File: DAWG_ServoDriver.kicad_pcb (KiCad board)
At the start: 2 copper layers, 70 x 84 mm, 155 parts, among them CN10 Conn_02x19_Odd_Even, CN7 Conn_02x19_Odd_Even, IC1 DRV8251ADDAR, IC2 DRV8251ADDAR, IC3 DRV8251ADDAR, IC4 DRV8251ADDAR, J1 Conn_01x05, J10 Screw_Terminal_01x02, J11 Conn_01x10, J12 Conn_01x08, J13 Conn_01x05, J14 Conn_01x06, J15 Conn_01x08, J16 Screw_Terminal_01x02, J17 Conn_01x03, J18 Conn_01x03, J19 Conn_01x03, J2 Screw_Terminal_01x02, J20 Conn_01x03, J21 Conn_01x03, J22 Conn_01x03, J23 Conn_01x03, J24 Conn_01x03, J25 Conn_01x03, J26 Conn_01x03, J27 Conn_01x03, J28 Conn_01x03, J29 Conn_01x03, J3 Conn_01x05, J30 Conn_01x03, J31 Conn_01x03, J32 Conn_01x03, J33 Conn_01x03, J34 Conn_01x03, J35 Conn_01x03, J36 Conn_01x03, J4 Conn_01x04_Pin, J5 Screw_Terminal_01x02, J6 Conn_01x03, J7 Screw_Terminal_01x02, J8 Screw_Terminal_01x02, J9 Conn_01x05, Q1 BSS138, Q10 BSS138, Q11 BSS138, Q12 BSS138, Q13 BSS138, Q14 BSS138, Q15 BSS138, Q16 BSS138, Q17 BSS138, Q18 BSS138, Q19 BSS138, Q2 BSS138, Q20 BSS138, Q3 BSS138, Q4 BSS138, Q5 BSS138, Q6 BSS138, Q7 BSS138, Q8 BSS138, Q9 BSS138, SW1 SW_Push, U1 TPS62177DQC, U2 STM32G431C8Tx, U3 LD1117S12TR_SOT223, U4 ICM-20602, U5 ICM-20602, Y1 Crystal_GND24

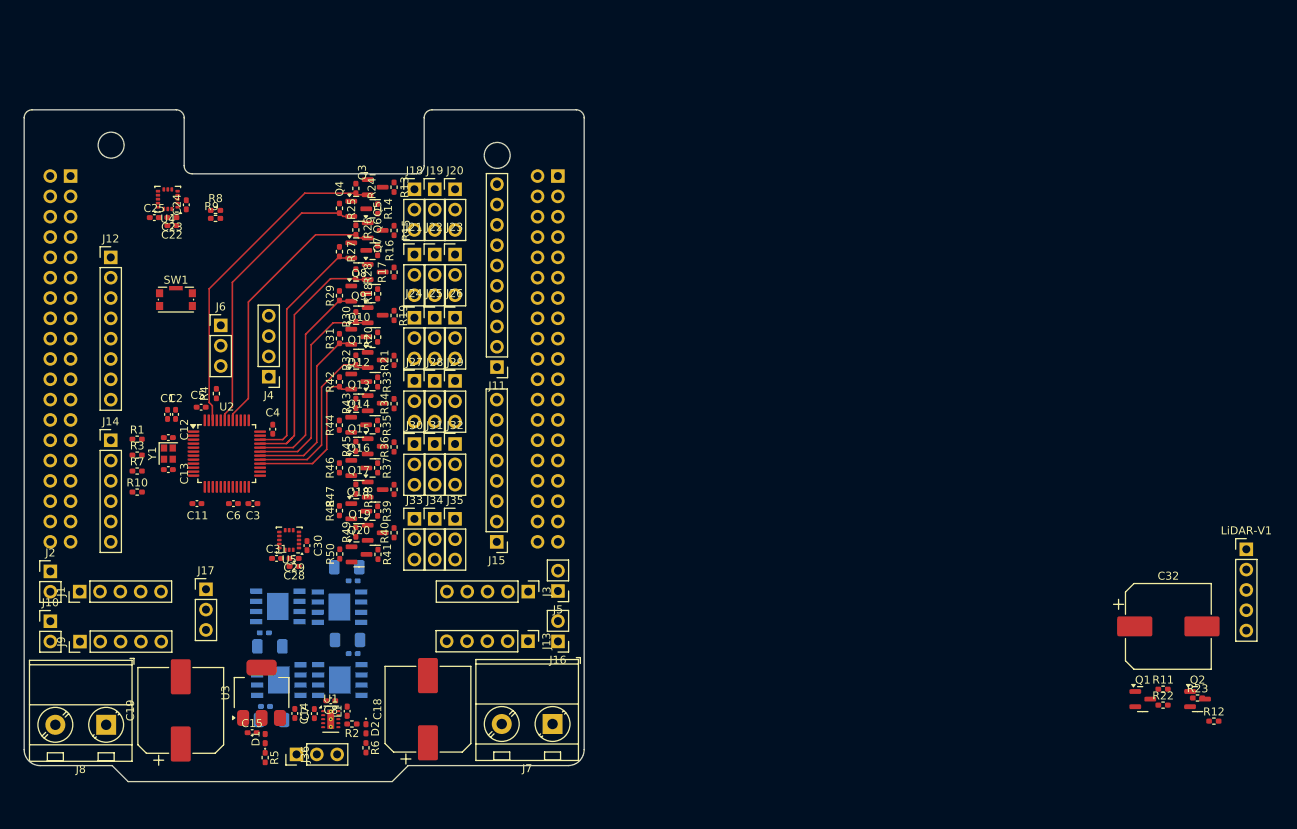
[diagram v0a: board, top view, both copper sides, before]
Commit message: Key components placed, Onion board begins.
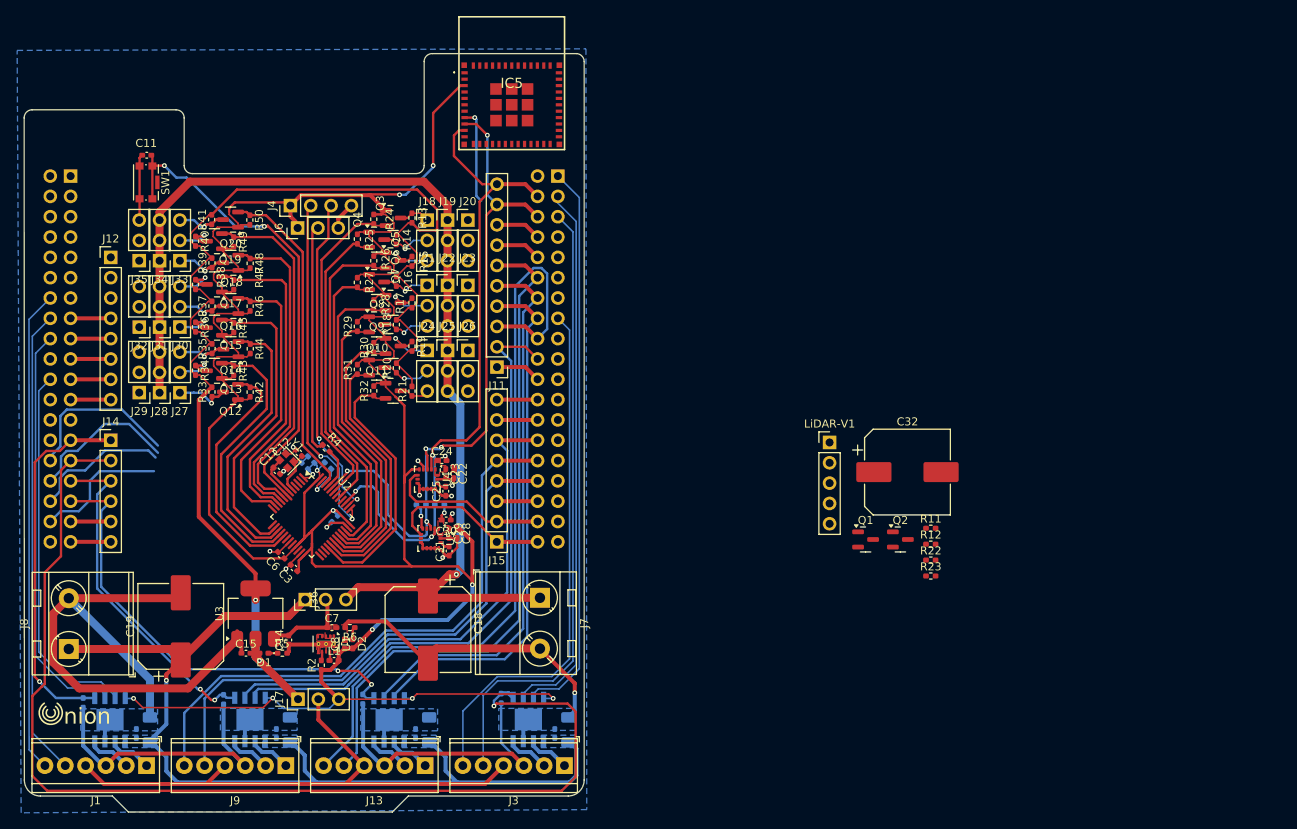
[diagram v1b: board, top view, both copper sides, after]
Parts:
- removed J10, J16, J2, J5: Screw_Terminal_01x02, Connector_PinHeader_2.54mm:PinHeader_1x02_P2.54mm_Vertical
- added IC5: ESP32-PICO-MINI-02-N8R2, Package_DFN_QFN:ESP32PICOMINI02N8R2, F.Cu at (84.0, 73.4)
- C1, C2, C4, C5, R1, R10, R3, R7, R8, R9: moved to B.Cu
- J1, J13, J3, J9: value Conn_01x05 -> Screw_Terminal_01x06; footprint Connector_PinHeader_2.54mm:PinHeader_1x05_P2.54mm_Vertical -> TerminalBlock_TE-Connectivity:TerminalBlock_TE_282834-6_1x06_P2.54mm_Horizontal
- moved R3 54.7 mm to (82.7, 147.6), turned to 90 degrees
- moved LiDAR-V1 53.8 mm to (123.8, 115.6)
- moved J35 51.0 mm to (37.5, 92.9), turned to 180 degrees
- moved C25 50.0 mm to (75.8, 121.7), turned to 90 degrees
- moved U4 47.7 mm to (73.5, 120.2), turned to -90 degrees
- moved J34 47.2 mm to (40.0, 92.9), turned to 180 degrees
- moved C22 46.9 mm to (76.8, 119.5), turned to -90 degrees
- moved C23 46.9 mm to (75.8, 119.5), turned to -90 degrees
- moved R41 46.7 mm to (46.5, 87.8), turned to 90 degrees
- moved R9 45.4 mm to (75.0, 123.4)
- moved C24 45.2 mm to (75.3, 117.9), turned to 0 degrees
- moved R8 44.9 mm to (72.7, 123.4), turned to 0 degrees
- moved Q20 44.8 mm to (48.9, 87.8), turned to 180 degrees
- moved R40 44.1 mm to (44.5, 90.5), turned to -90 degrees
- moved C11 44.0 mm to (38.4, 79.7), turned to 0 degrees
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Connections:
- net /I2C3_SCL renamed /I2C1_SCL_5V
- CN10 pad 1: unconnected-(CN10-Pin_1-Pad1) -> /PWM3/2_M2
- CN10 pad 10: unconnected-(CN10-Pin_10-Pad10) -> GND
- CN10 pad 11: /Mtr1_EncoderA -> unconnected-(CN10-Pin_11-Pad11)
- CN10 pad 12: unconnected-(CN10-Pin_12-Pad12) -> /Mtr4_EncoderA
- CN10 pad 13: /PWM2/1_M1 -> unconnected-(CN10-Pin_13-Pad13)
- CN10 pad 14: unconnected-(CN10-Pin_14-Pad14) -> /PWM2/3_M4
- CN10 pad 15: /PWM3/1_M1 -> /Mtr2_EncoderB
- CN10 pad 16: /Mtr1_EncoderZ -> /PWM3/2_M4
- CN10 pad 17: /Mtr1_EncoderB -> unconnected-(CN10-Pin_17-Pad17)
- CN10 pad 18: unconnected-(CN10-Pin_18-Pad18) -> /Mtr4_EncoderB
- CN10 pad 19: /PWM3/2_M2 -> unconnected-(CN10-Pin_19-Pad19)
- CN10 pad 20: unconnected-(CN10-Pin_20-Pad20) -> /PWM1/1_M3
- CN10 pad 21: Net-(CN10-Pin_21) -> unconnected-(CN10-Pin_21-Pad21)
- CN10 pad 22: unconnected-(CN10-Pin_22-Pad22) -> Net-(CN10-Pin_22)
- CN10 pad 23: Net-(CN10-Pin_23) -> unconnected-(CN10-Pin_23-Pad23)
- CN10 pad 24: unconnected-(CN10-Pin_24-Pad24) -> Net-(CN10-Pin_24)
- CN10 pad 25: Net-(CN10-Pin_25) -> unconnected-(CN10-Pin_25-Pad25)
- CN10 pad 26: unconnected-(CN10-Pin_26-Pad26) -> Net-(CN10-Pin_26)
- CN10 pad 27: /PWM4/1_M2 -> unconnected-(CN10-Pin_27-Pad27)
- CN10 pad 28: unconnected-(CN10-Pin_28-Pad28) -> /PWM1/2_M3
- CN10 pad 29: /Mtr2_EncoderA -> unconnected-(CN10-Pin_29-Pad29)
- CN10 pad 3: /I2C1_SCL -> /PWM4/1_M2
- CN10 pad 30: unconnected-(CN10-Pin_30-Pad30) -> /Mtr3_EncoderB
- CN10 pad 31: /Mtr2_EncoderB -> unconnected-(CN10-Pin_31-Pad31)
- CN10 pad 32: unconnected-(CN10-Pin_32-Pad32) -> /Mtr3_EncoderA
- CN10 pad 33: Net-(CN10-Pin_33) -> unconnected-(CN10-Pin_33-Pad33)
- CN10 pad 34: unconnected-(CN10-Pin_34-Pad34) -> Net-(CN10-Pin_34)
- CN10 pad 35: /IMU2_INT -> unconnected-(CN10-Pin_35-Pad35)
- CN10 pad 36: unconnected-(CN10-Pin_36-Pad36) -> /IMU1_INT
- CN10 pad 37: /IMU1_INT -> unconnected-(CN10-Pin_37-Pad37)
- CN10 pad 38: unconnected-(CN10-Pin_38-Pad38) -> /IMU2_INT
- CN10 pad 4: unconnected-(CN10-Pin_4-Pad4) -> /I2C1_SCL
- CN10 pad 5: /I2C1_SDA -> /Mtr2_EncoderA
- CN10 pad 6: unconnected-(CN10-Pin_6-Pad6) -> /I2C1_SDA
- CN10 pad 7: Net-(CN10-Pin_7) -> unconnected-(CN10-Pin_7-Pad7)
- CN10 pad 8: unconnected-(CN10-Pin_8-Pad8) -> Net-(CN10-Pin_8)
- CN10 pad 9: GND -> unconnected-(CN10-Pin_9-Pad9)
- CN7 pad 14: unconnected-(CN7-Pin_14-Pad14) -> /Mtr1_EncoderB
- CN7 pad 15: unconnected-(CN7-Pin_15-Pad15) -> +3.3V
- CN7 pad 16: +3.3V -> /Mtr1_EncoderA
- CN7 pad 17: /Mtr4_EncoderA -> +5V
- CN7 pad 18: +5V -> /PWM2/1_M1
- CN7 pad 19: unconnected-(CN7-Pin_19-Pad19) -> GND
- CN7 pad 20: GND -> unconnected-(CN7-Pin_20-Pad20)
- CN7 pad 21: /Mtr4_EncoderB -> GND
- CN7 pad 22: GND -> /PWM3/1_M1
- CN7 pad 23: /Mtr4_EncoderZ -> Net-(CN7-Pin_23)
- CN7 pad 24: Net-(CN7-Pin_24) -> unconnected-(CN7-Pin_24-Pad24)
- CN7 pad 27: unconnected-(CN7-Pin_27-Pad27) -> /IsenseM1
- CN7 pad 28: /IsenseM1 -> unconnected-(CN7-Pin_28-Pad28)
- CN7 pad 29: unconnected-(CN7-Pin_29-Pad29) -> /IsenseM2
- CN7 pad 30: /IsenseM2 -> unconnected-(CN7-Pin_30-Pad30)
- CN7 pad 31: unconnected-(CN7-Pin_31-Pad31) -> /IsenseM3
- CN7 pad 32: /IsenseM3 -> unconnected-(CN7-Pin_32-Pad32)
- CN7 pad 33: unconnected-(CN7-Pin_33-Pad33) -> /IsenseM4
- CN7 pad 34: /IsenseM4 -> unconnected-(CN7-Pin_34-Pad34)
- CN7 pad 35: unconnected-(CN7-Pin_35-Pad35) -> Net-(CN7-Pin_35)
- CN7 pad 36: Net-(CN7-Pin_36) -> unconnected-(CN7-Pin_36-Pad36)
- CN7 pad 37: unconnected-(CN7-Pin_37-Pad37) -> Net-(CN7-Pin_37)
- CN7 pad 38: Net-(CN7-Pin_38) -> unconnected-(CN7-Pin_38-Pad38)
- IC1 pad 6: /V_M1B -> /V_M1A
- IC1 pad 8: /V_M1A -> /V_M1B
- IC2 pad 6: /V_M2B -> /V_M2A
- IC2 pad 8: /V_M2A -> /V_M2B
- IC3 pad 6: /V_M3B -> /V_M3A
- IC3 pad 8: /V_M3A -> /V_M3B
- IC4 pad 6: /V_M4B -> /V_M4A
- IC4 pad 8: /V_M4A -> /V_M4B
- J1 pad 1: /V_encoder -> /V_M1A
- J1 pad 2: /Mtr1_EncoderA -> /V_M1B
- J1 pad 3: /Mtr1_EncoderB -> GND
- J1 pad 4: /Mtr1_EncoderZ -> /V_encoder
- J1 pad 5: GND -> /Mtr1_EncoderA
- J11 pad 1: Net-(CN10-Pin_21) -> Net-(CN10-Pin_22)
- J11 pad 2: /PWM3/2_M2 -> /PWM1/1_M3
- J11 pad 3: /Mtr1_EncoderB -> /Mtr4_EncoderB
- J11 pad 4: /PWM3/1_M1 -> /PWM3/2_M4
- J11 pad 5: /PWM2/1_M1 -> /PWM2/3_M4
- J11 pad 6: /Mtr1_EncoderA -> /Mtr4_EncoderA
- J11 pad 8: Net-(CN10-Pin_7) -> Net-(CN10-Pin_8)
- J12 pad 8: Net-(CN7-Pin_24) -> Net-(CN7-Pin_23)
- J13 pad 1: /V_encoder -> /V_M4A
- J13 pad 2: /Mtr4_EncoderA -> /V_M4B
- J13 pad 3: /Mtr4_EncoderB -> GND
- J13 pad 4: /Mtr4_EncoderZ -> /V_encoder
- J13 pad 5: GND -> /Mtr4_EncoderA
- J14 pad 5: Net-(CN7-Pin_36) -> Net-(CN7-Pin_35)
- J14 pad 6: Net-(CN7-Pin_38) -> Net-(CN7-Pin_37)
- J15 pad 1: /IMU1_INT -> /IMU2_INT
- J15 pad 2: /IMU2_INT -> /IMU1_INT
- J15 pad 3: Net-(CN10-Pin_33) -> Net-(CN10-Pin_34)
- J15 pad 4: /Mtr2_EncoderB -> /Mtr3_EncoderA
- J15 pad 5: /Mtr2_EncoderA -> /Mtr3_EncoderB
- J15 pad 6: /PWM4/1_M2 -> /PWM1/2_M3
- J15 pad 7: Net-(CN10-Pin_25) -> Net-(CN10-Pin_26)
- J15 pad 8: Net-(CN10-Pin_23) -> Net-(CN10-Pin_24)
- J3 pad 1: /V_encoder -> /V_M2A
- J3 pad 2: /Mtr2_EncoderA -> /V_M2B
- J3 pad 3: /Mtr2_EncoderB -> GND
- J3 pad 4: /Mtr2_EncoderZ -> /V_encoder
- J3 pad 5: GND -> /Mtr2_EncoderA
- J9 pad 1: /V_encoder -> /V_M3A
- J9 pad 2: /Mtr3_EncoderA -> /V_M3B
- J9 pad 3: /Mtr3_EncoderB -> GND
- J9 pad 4: /Mtr3_EncoderZ -> /V_encoder
- J9 pad 5: GND -> /Mtr3_EncoderA
- LiDAR-V1 pad 3: /I2C3_SDA -> /I2C1_SDA_5V
- Q1 pad 2: /I2C3_SDA -> /I2C1_SDA_5V
- Q10 pad 2: /PWM1/1 -> /PWM15/2
- Q11 pad 2: /PWM15/2 -> /PWM15/1
- Q12 pad 2: /PWM15/1 -> /PWM3/4
- Q14 pad 2: /PWM3/4 -> /PWM3/2
- Q15 pad 2: Net-(Q15-S) -> /PWM3/1
- Q16 pad 2: Net-(Q16-S) -> /PWM2/4
- Q17 pad 2: Net-(Q17-S) -> /PWM2/3
- Q18 pad 2: Net-(Q18-S) -> /PWM2/2
- Q19 pad 2: Net-(Q19-S) -> /PWM2/1
- Q20 pad 2: Net-(Q20-S) -> /PWM4/4
- Q3 pad 2: /PWM4/4 -> /PWM4/1
- Q4 pad 2: /PWM4/1 -> /PWM16/1
- Q5 pad 2: /PWM16/1 -> /PWM4/2
- Q6 pad 2: /PWM4/2 -> /PWM1/4
- Q7 pad 2: /PWM1/4 -> /PWM1/3
- Q8 pad 2: /PWM1/3 -> /PWM1/2
- Q9 pad 2: /PWM1/2 -> /PWM1/1
- R22 pad 1: /I2C3_SDA -> /I2C1_SDA_5V
- R24 pad 1: /PWM4/4 -> /PWM4/1
- R25 pad 1: /PWM4/1 -> /PWM16/1
- R26 pad 1: /PWM16/1 -> /PWM4/2
- R27 pad 1: /PWM4/2 -> /PWM1/4
- R28 pad 1: /PWM1/4 -> /PWM1/3
- R29 pad 1: /PWM1/3 -> /PWM1/2
- R30 pad 1: /PWM1/2 -> /PWM1/1
- R31 pad 1: /PWM1/1 -> /PWM15/2
- R32 pad 1: /PWM15/2 -> /PWM15/1
- R42 pad 1: /PWM15/1 -> /PWM3/4
- R44 pad 1: /PWM3/4 -> /PWM3/2
- R45 pad 1: Net-(Q15-S) -> /PWM3/1
- R46 pad 1: Net-(Q16-S) -> /PWM2/4
- R47 pad 1: Net-(Q17-S) -> /PWM2/3
- R48 pad 1: Net-(Q18-S) -> /PWM2/2
- R49 pad 1: Net-(Q19-S) -> /PWM2/1
- R50 pad 1: Net-(Q20-S) -> /PWM4/4
- U1 pad 11: unconnected-(U1-PAD-Pad11)_2 -> GND
- U2 pad 11: unconnected-(U2-PA3-Pad11) -> /PWM2/4
- U2 pad 12: /PWM3/2 -> unconnected-(U2-PA4-Pad12)
- U2 pad 13: /PWM2/1 -> unconnected-(U2-PA5-Pad13)
- U2 pad 15: unconnected-(U2-PA7-Pad15) -> /PWM3/2
- U2 pad 25: /PWM2/4 -> unconnected-(U2-PB11-Pad25)
- U2 pad 42: /I2C3_SDA -> unconnected-(U2-PB5-Pad42)
- U2 pad 8: unconnected-(U2-PA0-Pad8) -> /PWM2/1
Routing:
- net +3.3V: track 0.00 -> 377.4 mm, vias 0 -> 13
- net GND: track 0.00 -> 269.5 mm, vias 0 -> 14
- net +5V: track 0.00 -> 154.9 mm, vias 0 -> 2
- net /IsenseM2: track 0.00 -> 138.4 mm, vias 0 -> 1
- net V_Servo: track 0.00 -> 137.4 mm, vias 0 -> 1
- net V_DCMTR: track 0.00 -> 119.9 mm, vias 0 -> 1
- net /Mtr4_EncoderB: track 0.00 -> 95.7 mm
- net /I2C1_SDA: track 0.00 -> 88.8 mm, vias 0 -> 5
- net /I2C1_SCL: track 0.00 -> 85.6 mm, vias 0 -> 3
- net /Mtr4_EncoderA: track 0.00 -> 83.7 mm
- net /Mtr2_EncoderA: track 0.00 -> 78.1 mm
- net /PWM1/1_M3: track 0.00 -> 75.6 mm
- net /Mtr3_EncoderB: track 0.00 -> 73.1 mm
- net /V_encoder: track 0.00 -> 71.3 mm
- net /PWM3/2_M2: track 0.00 -> 70.2 mm
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- added copper zone on F.Cu, net +3.3V
- added copper zone on F.Cu, net +BATT
- added copper zone on B.Cu, net GND
- added copper zone on F.Cu, net GND
- added copper zone on B.Cu, net V_DCMTR
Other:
- board size 70 x 84 mm -> 70 x 94.8 mm
- board text added: "nion"

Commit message: Cosmetic changes
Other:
- board text added: "EN_B EN_A V_EN GND M_B M_A"
- board text added: "V DCMTR"
- board text added: "V Servo"
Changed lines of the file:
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@@
 		(tags "capacitor handsolder")
 		(property "Reference" "C11"
-			(at -0.0675 -1.5 0)
+			(at 2.6 0 0)
 			(layer "F.SilkS")
 			(effects
@@
 	)
 	(gr_arc
-		(start 27 148.6)
-		(mid 26.4 150.399998)
-		(end 25.8 148.6)
+		(start 27.3 76.149998)
+		(mid 26.705056 78.433675)
+		(end 25.909053 76.212072)
 		(stroke
-			(width 0.2)
+			(width 0.3)
 			(type default)
 		)
@@
 	)
 	(gr_arc
-		(start 27.2 148.200001)
-		(mid 26.4 150.842218)
-		(end 25.599999 148.200001)
+		(start 27.55 75.65)
+		(mid 26.705495 78.991477)
+		(end 25.655786 75.708678)
 		(stroke
-			(width 0.2)
+			(width 0.4)
 			(type default)
 		)
@@
 	)
 	(gr_arc
-		(start 26.8 149)
-		(mid 26.4 149.965685)
-		(end 26 149)
+		(start 27.144975 76.705023)
+		(mid 26.65 77.899998)
+		(end 26.155025 76.705023)
 		(stroke
-			(width 0.2)
+			(width 0.25)
 			(type default)
 		)
@@
 		)
 	)
-	(gr_text "nion"
-		(at 28 151 0)
+	(gr_text "EN_B EN_A V_EN GND M_B M_A"
+		(at 24.5 152.05 0)
+		(layer "F.SilkS")
+		(effects
+			(font
+				(size 0.6 0.63)
+				(thickness 0.15)
+				(bold yes)
+			)
+			(justify left bottom)
+		)
+	)
+	(gr_text "V Servo"
+		(at 82.1 147.15 0)
+		(layer "F.SilkS")
+		(effects
+			(font
+				(size 1.5 1.5)
+				(thickness 0.3)
+				(bold yes)
+			)
+			(justify left bottom)
+		)
+	)
+	(gr_text "V DCMTR"
+		(at 26.2 147.4 0)
+		(layer "F.SilkS")
+		(effects
+			(font
+				(size 1.5 1.5)
+				(thickness 0.3)
+				(bold yes)
+			)
+			(justify left bottom)
+		)
+	)
+	(gr_text "EN_B EN_A V_EN GND M_B M_A"
+		(at 41.7 152.1 0)
 		(layer "F.SilkS")
 		(effects
 			(font
+				(size 0.6 0.63)
+				(thickness 0.15)
+				(bold yes)
+			)
+			(justify left bottom)
+		)
+	)
+	(gr_text "EN_B EN_A V_EN GND M_B M_A"
+		(at 76.8 152.05 0)
+		(layer "F.SilkS")
+		(effects
+			(font
+				(size 0.6 0.63)
+				(thickness 0.15)
+				(bold yes)
+			)
+			(justify left bottom)
+		)
+	)
+	(gr_text "EN_B EN_A V_EN GND M_B M_A"
+		(at 59.4 152.1 0)
+		(layer "F.SilkS")
+		(effects
+			(font
+				(size 0.6 0.63)
+				(thickness 0.15)
+				(bold yes)
+			)
+			(justify left bottom)
+		)
+	)
+	(gr_text "nion"
+		(at 28.6 78.799998 0)
+		(layer "F.SilkS" knockout)
+		(effects
+			(font
 				(size 2 2)
-				(thickness 0.2)
+				(thickness 0.3)
 			)
 			(justify left bottom)
@@
 		(members "cc4378c6-6c7e-484c-aff8-dc50a309752f" "f3348520-9b0f-4b79-b100-57973a9e689c")
 	)
+	(group ""
+		(members "28dae0e6-ecd4-4664-9976-c7416e2b5326" "33c00be5-3335-4219-ad12-b52f86d37b1e"
+			"4fc859f8-7f1f-4527-b22f-c6be2e80f9df" "c791974b-7826-4446-81e5-399a6a863a32"
+		)
+	)
 )
